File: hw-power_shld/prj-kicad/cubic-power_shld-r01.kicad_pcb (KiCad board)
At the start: 2 copper layers, 13.3 x 24.5 mm, 17 parts

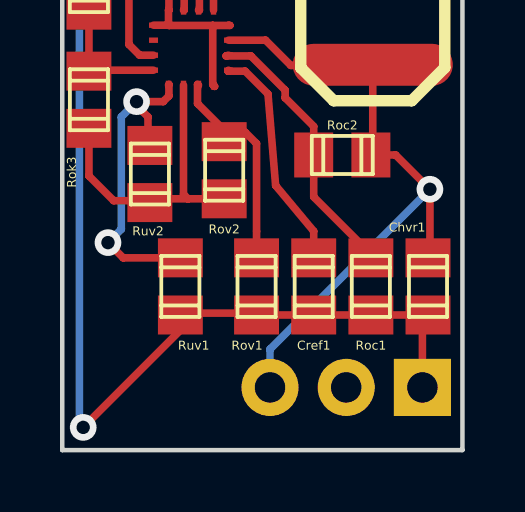
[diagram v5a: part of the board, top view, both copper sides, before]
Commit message: missing a net
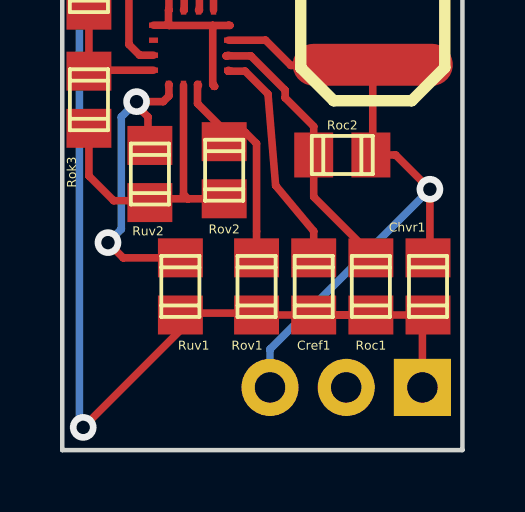
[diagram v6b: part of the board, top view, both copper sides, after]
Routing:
- net GND: track 51.0 -> 53.1 mm
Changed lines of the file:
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@@
   (general
     (links 35)
-    (no_connects 1)
+    (no_connects 0)
     (area 142.174999 67.174999 184.12714 107.325001)
     (thickness 1.6)
     (drawings 20)
-    (tracks 127)
+    (tracks 130)
     (zones 0)
     (modules 17)
@@
   (gr_line (start 142.25 75) (end 150 75) (angle 90) (layer Dwgs.User) (width 0.15))
   (gr_line (start 142.25 75) (end 142.25 99.5) (angle 90) (layer Dwgs.User) (width 0.15))
+  (segment (start 179.197 94.996) (end 177.292 94.996) (width 0.254) (layer F.Cu) (net 1))
+  (segment (start 177.292 94.996) (end 177.2285 94.996) (width 0.254) (layer F.Cu) (net 1))
+  (segment (start 177.2285 94.996) (end 177.292 94.996) (width 0.254) (layer F.Cu) (net 1))
   (segment (start 172.452 84.836) (end 172.452 85.33) (width 0.254) (layer F.Cu) (net 1))
   (segment (start 172.452 85.33) (end 172.466 85.344) (width 0.254) (layer F.Cu) (net 1))
@@
   (segment (start 175.387 89.281) (end 175.006 88.9) (width 0.254) (layer F.Cu) (net 2))
   (segment (start 175.387 92.202) (end 175.387 89.281) (width 0.254) (layer F.Cu) (net 2))
-  (segment (start 174.244 80.645) (end 174.244 79.8195) (width 0.254) (layer F.Cu) (net 3) (status 400000))
-  (segment (start 180.848 77.47) (end 180.915 77.09) (width 0.254) (layer F.Cu) (net 3) (status C00000))
-  (segment (start 178.1175 80.2005) (end 180.848 77.47) (width 0.254) (layer F.Cu) (net 3) (status C00000))
-  (segment (start 178.1175 80.391) (end 178.1175 80.2005) (width 0.254) (layer F.Cu) (net 3) (status C00000))
-  (segment (start 177.165 79.4385) (end 178.1175 80.391) (width 0.254) (layer F.Cu) (net 3) (status 800000))
+  (segment (start 174.244 80.645) (end 174.244 79.8195) (width 0.254) (layer F.Cu) (net 3))
+  (segment (start 180.848 77.47) (end 180.915 77.09) (width 0.254) (layer F.Cu) (net 3))
+  (segment (start 178.1175 80.2005) (end 180.848 77.47) (width 0.254) (layer F.Cu) (net 3))
+  (segment (start 178.1175 80.391) (end 178.1175 80.2005) (width 0.254) (layer F.Cu) (net 3))
+  (segment (start 177.165 79.4385) (end 178.1175 80.391) (width 0.254) (layer F.Cu) (net 3))
   (segment (start 174.625 79.4385) (end 177.165 79.4385) (width 0.254) (layer F.Cu) (net 3))
   (segment (start 174.244 79.8195) (end 174.625 79.4385) (width 0.254) (layer F.Cu) (net 3))
-  (segment (start 176.2125 80.772) (end 176.2125 81.915) (width 0.254) (layer F.Cu) (net 4) (status 400000))
-  (segment (start 175.5775 82.55) (end 174.244 82.55) (width 0.254) (layer F.Cu) (net 4) (status 800000))
+  (segment (start 176.2125 80.772) (end 176.2125 81.915) (width 0.254) (layer F.Cu) (net 4))
+  (segment (start 175.5775 82.55) (end 174.244 82.55) (width 0.254) (layer F.Cu) (net 4))
   (segment (start 176.2125 81.915) (end 175.5775 82.55) (width 0.254) (layer F.Cu) (net 4))
-  (segment (start 174.244 82.55) (end 174.244 82.9945) (width 0.254) (layer F.Cu) (net 4) (status C00000))
-  (segment (start 173.482 84.836) (end 173.452 84.836) (width 0.254) (layer F.Cu) (net 4) (status C00000))
-  (segment (start 173.482 83.7565) (end 173.482 84.836) (width 0.254) (layer F.Cu) (net 4) (status 800000))
-  (segment (start 174.244 82.9945) (end 173.482 83.7565) (width 0.254) (layer F.Cu) (net 4) (status 400000))
+  (segment (start 174.244 82.55) (end 174.244 82.9945) (width 0.254) (layer F.Cu) (net 4))
+  (segment (start 173.482 84.836) (end 173.452 84.836) (width 0.254) (layer F.Cu) (net 4))
+  (segment (start 173.482 83.7565) (end 173.482 84.836) (width 0.254) (layer F.Cu) (net 4))
+  (segment (start 174.244 82.9945) (end 173.482 83.7565) (width 0.254) (layer F.Cu) (net 4))
   (segment (start 177.292 93.091) (end 177.292 92.202) (width 0.254) (layer F.Cu) (net 5))
   (segment (start 174.4345 86.868) (end 174.452 86.836) (width 0.254) (layer F.Cu) (net 5))

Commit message: ...
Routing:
- net GND: track 53.1 -> 22.3 mm, vias 2 -> 0
- net N-0000015: track 22.0 -> 20.2 mm
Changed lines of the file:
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@@
   (general
     (links 35)
-    (no_connects 0)
+    (no_connects 1)
     (area 142.174999 67.174999 184.12714 107.325001)
     (thickness 1.6)
     (drawings 20)
-    (tracks 130)
+    (tracks 120)
     (zones 0)
     (modules 17)
@@
     (user_trace_width 0.3048)
     (trace_clearance 0.1524)
-    (zone_clearance 0.2032)
-    (zone_45_only no)
+    (zone_clearance 0.508)
+    (zone_45_only yes)
     (trace_min 0.1524)
     (segment_width 0.15)
@@
   (segment (start 172.466 84.074) (end 172.466 84.836) (width 0.254) (layer F.Cu) (net 1))
   (segment (start 171.6405 83.2485) (end 172.466 84.074) (width 0.254) (layer F.Cu) (net 1))
-  (segment (start 172.847 94.996) (end 172.847 95.504) (width 0.254) (layer F.Cu) (net 1))
-  (segment (start 171.6405 80.7085) (end 171.6405 80.8355) (width 0.254) (layer F.Cu) (net 1))
-  (segment (start 171.6405 79.5655) (end 171.6405 80.7085) (width 0.254) (layer F.Cu) (net 1))
-  (segment (start 169.4815 77.4065) (end 171.6405 79.5655) (width 0.254) (layer F.Cu) (net 1))
-  (via (at 169.4815 77.4065) (size 0.889) (layers F.Cu B.Cu) (net 1))
-  (segment (start 169.4815 77.47) (end 169.4815 77.4065) (width 0.254) (layer B.Cu) (net 1))
-  (segment (start 169.4815 98.6155) (end 169.4815 77.47) (width 0.254) (layer B.Cu) (net 1))
-  (segment (start 169.6085 98.7425) (end 169.4815 98.6155) (width 0.254) (layer B.Cu) (net 1))
-  (via (at 169.6085 98.7425) (size 0.889) (layers F.Cu B.Cu) (net 1))
-  (segment (start 172.847 95.504) (end 169.6085 98.7425) (width 0.254) (layer F.Cu) (net 1))
   (segment (start 180.915 97.41) (end 180.915 95.183) (width 0.254) (layer F.Cu) (net 1))
   (segment (start 180.728 94.996) (end 177.292 94.996) (width 0.254) (layer F.Cu) (net 1))
@@
   (segment (start 174.4345 86.868) (end 174.452 86.836) (width 0.254) (layer F.Cu) (net 5))
   (segment (start 175.006 86.868) (end 174.4345 86.868) (width 0.254) (layer F.Cu) (net 5))
-  (segment (start 175.768 87.63) (end 175.006 86.868) (width 0.254) (layer F.Cu) (net 5))
-  (segment (start 176.022 90.678) (end 175.768 87.63) (width 0.254) (layer F.Cu) (net 5))
-  (segment (start 177.292 92.202) (end 176.022 90.678) (width 0.254) (layer F.Cu) (net 5))
+  (segment (start 176.0855 88.9) (end 175.006 86.868) (width 0.254) (layer F.Cu) (net 5))
+  (segment (start 176.0855 91.059) (end 176.0855 88.9) (width 0.254) (layer F.Cu) (net 5))
+  (segment (start 177.292 92.202) (end 176.0855 91.059) (width 0.254) (layer F.Cu) (net 5))
   (segment (start 174.452 85.836) (end 175.6885 85.836) (width 0.254) (layer F.Cu) (net 6))
   (segment (start 178.3715 86.6775) (end 179.2605 86.65464) (width 0.254) (layer F.Cu) (net 6))
@@
   (segment (start 179.2605 86.65464) (end 179.2605 89.662) (width 0.254) (layer F.Cu) (net 6))
   (segment (start 179.2605 89.662) (end 179.197 89.662) (width 0.254) (layer F.Cu) (net 6))
-  (segment (start 179.197 89.662) (end 180.0225 89.662) (width 0.254) (layer F.Cu) (net 6))
-  (segment (start 180.0225 89.662) (end 181.1655 90.805) (width 0.254) (layer F.Cu) (net 6))
+  (segment (start 179.197 89.662) (end 179.197 89.5985) (width 0.254) (layer F.Cu) (net 6) (status 400000))
+  (segment (start 179.197 89.5985) (end 180.0225 91.313) (width 0.254) (layer F.Cu) (net 6))
   (segment (start 175.835 97.41) (end 175.835 96.1355) (width 0.254) (layer B.Cu) (net 6))
   (segment (start 181.1655 93.218) (end 181.102 93.091) (width 0.254) (layer F.Cu) (net 6))
-  (segment (start 181.1655 90.805) (end 181.1655 93.218) (width 0.254) (layer F.Cu) (net 6))
-  (via (at 181.1655 90.805) (size 0.889) (layers F.Cu B.Cu) (net 6))
-  (segment (start 175.835 96.1355) (end 181.1655 90.805) (width 0.254) (layer B.Cu) (net 6))
+  (segment (start 180.0225 91.313) (end 181.1655 93.218) (width 0.254) (layer F.Cu) (net 6))
+  (via (at 180.0225 91.313) (size 0.889) (layers F.Cu B.Cu) (net 6))
+  (segment (start 175.835 96.1355) (end 180.0225 91.313) (width 0.254) (layer B.Cu) (net 6))
   (segment (start 175.835 77.09) (end 174.116 77.09) (width 0.254) (layer F.Cu) (net 7))
   (segment (start 172.974 84.836) (end 172.952 84.836) (width 0.254) (layer F.Cu) (net 7))
@@
   (segment (start 175.1965 86.36) (end 174.371 86.36) (width 0.254) (layer F.Cu) (net 12))
   (segment (start 176.3395 87.503) (end 175.1965 86.36) (width 0.254) (layer F.Cu) (net 12))
-  (segment (start 176.3395 87.757) (end 176.3395 87.503) (width 0.254) (layer F.Cu) (net 12))
-  (segment (start 177.292 88.7095) (end 176.3395 87.757) (width 0.254) (layer F.Cu) (net 12))
-  (segment (start 177.292 89.662) (end 177.292 91.059) (width 0.254) (layer F.Cu) (net 12))
+  (segment (start 176.4665 87.63) (end 176.3395 87.503) (width 0.254) (layer F.Cu) (net 12))
+  (segment (start 177.292 88.7095) (end 176.4665 87.63) (width 0.254) (layer F.Cu) (net 12))
+  (segment (start 177.292 89.662) (end 178.2445 91.3765) (width 0.254) (layer F.Cu) (net 12) (status 400000))
   (segment (start 179.324 93.091) (end 179.197 93.091) (width 0.254) (layer F.Cu) (net 12))
-  (segment (start 177.292 91.059) (end 179.324 93.091) (width 0.254) (layer F.Cu) (net 12))
+  (segment (start 178.2445 91.3765) (end 179.324 93.091) (width 0.254) (layer F.Cu) (net 12))
   (segment (start 173.952 84.836) (end 173.952 84.0485) (width 0.254) (layer F.Cu) (net 13))
   (segment (start 177.419 83.693) (end 179.2605 83.65236) (width 0.254) (layer F.Cu) (net 13))

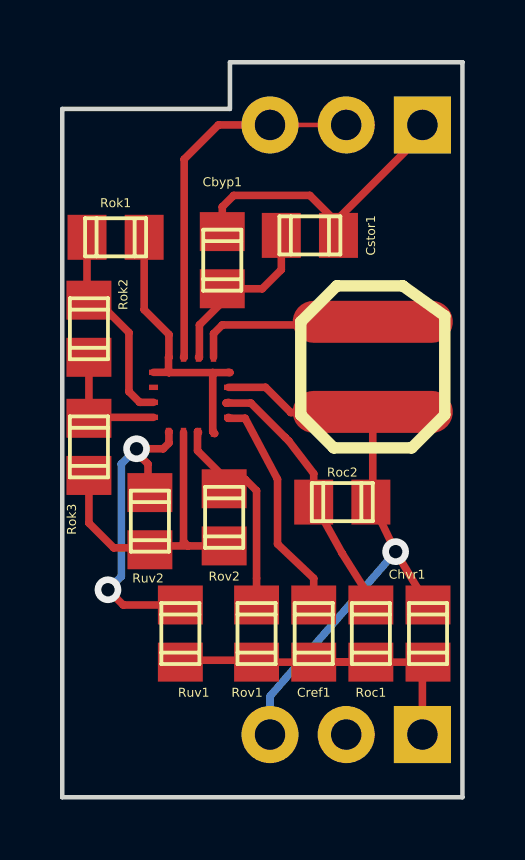
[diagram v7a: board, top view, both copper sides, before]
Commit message: change footprint qfn and re-route
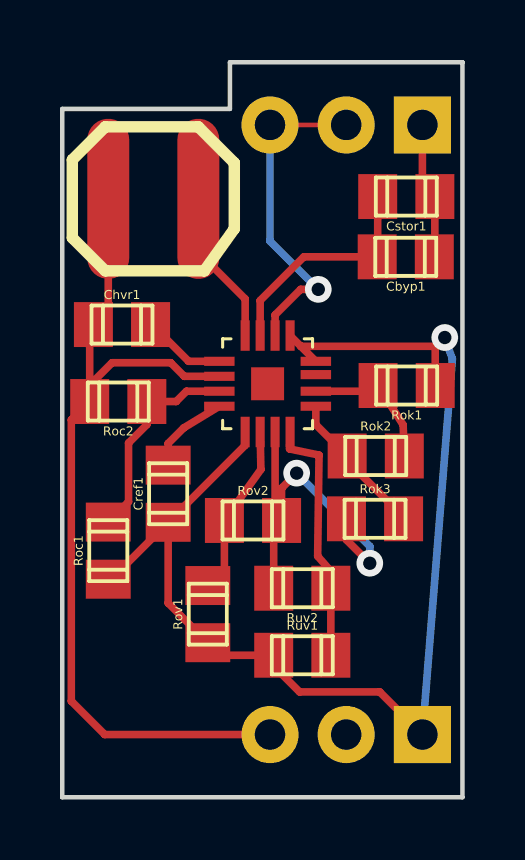
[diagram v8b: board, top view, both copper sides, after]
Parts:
- removed the ? at (174.8, 84.8)
- added bq25504_1: BQ25504, QFN16, F.Cu at (175.8, 85.7)
- moved Chvr1 14.5 mm to (170.9, 83.7), turned to 0 degrees
- moved Rok1 10.9 mm to (180.4, 85.8)
- moved Rok2 10.5 mm to (179.4, 88.1), turned to 0 degrees
- moved Rok3 9.83 mm to (179.3, 90.2), turned to 0 degrees
- moved ? 9.21 mm to (171.9, 79.6), turned to 0 degrees
- moved Roc1 9.18 mm to (170.4, 91.3)
- moved Roc2 8.19 mm to (170.8, 86.3), turned to 180 degrees
- moved Cref1 6.73 mm to (172.4, 89.4)
- moved Cbyp1 6.12 mm to (180.4, 81.5), turned to 180 degrees
- moved Ruv2 5.55 mm to (176.9, 92.5), turned to 180 degrees
- moved Ruv1 4.13 mm to (176.9, 94.8), turned to 0 degrees
- moved Cstor1 3.46 mm to (180.4, 79.5)
- moved Rov1 1.75 mm to (173.8, 93.4)
- moved Rov2 0.97 mm to (175.3, 90.3), turned to 0 degrees
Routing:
- net GND: track 22.3 -> 44.0 mm, vias 0 -> 1
- net N-0000015: track 20.2 -> 29.7 mm, vias 1 -> 0
- net N-0000012: track 9.69 -> 4.58 mm
- net N-0000014: track 7.62 -> 2.85 mm
- net N-000006: track 9.93 -> 13.0 mm, vias 0 -> 2
- net N-000005: track 10.9 -> 8.41 mm, vias 2 -> 0
- net N-000003: track 6.82 -> 4.75 mm
- net N-000007: track 9.13 -> 7.11 mm
- net N-0000013: track 6.01 -> 7.69 mm
- net N-000002: track 12.6 -> 11.2 mm, vias 0 -> 1
- net N-000001: track 7.01 -> 5.74 mm
- net N-000008: track 6.24 -> 5.20 mm
- net N-000004: track 4.22 -> 4.96 mm
